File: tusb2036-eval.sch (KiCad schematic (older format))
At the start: 55 parts, among them J1 USB_B_Micro, J2 USB_A, J3 USB_A, J4 USB_A, SW1 RESET, U1 TUSB2036, U2 TPS76333, U3 TPS2044D, U4 SN75240, U5 SN75240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

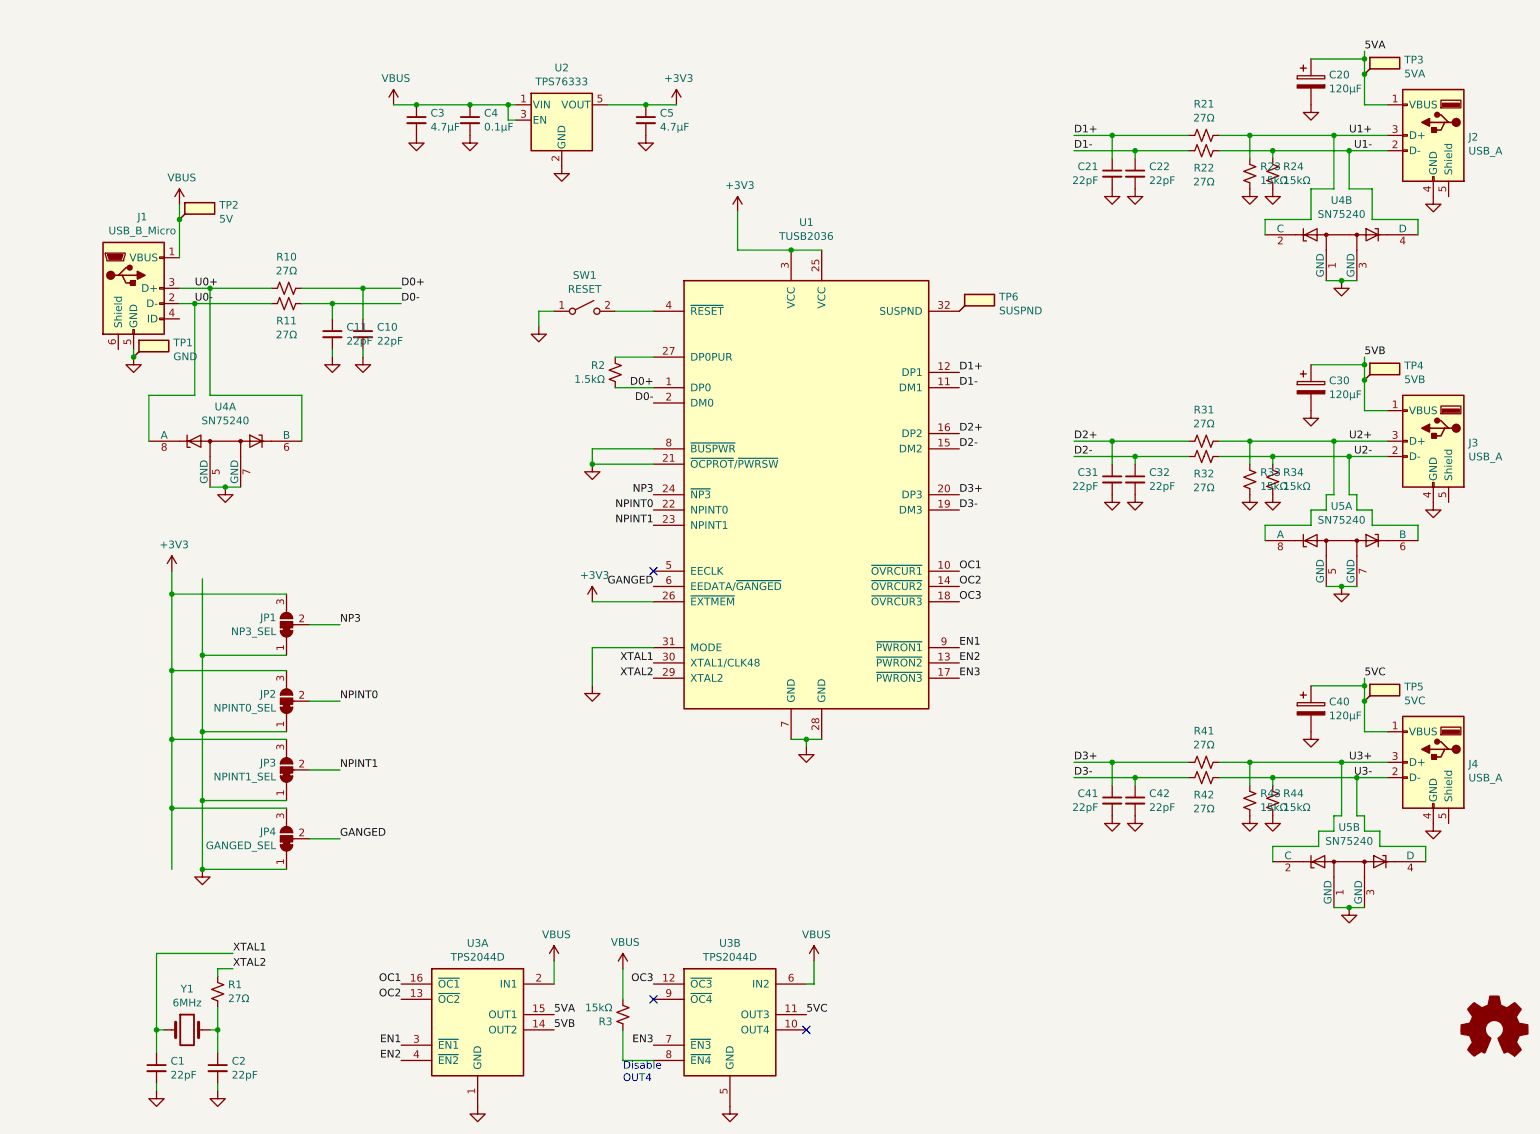
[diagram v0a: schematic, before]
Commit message: Add LEDs
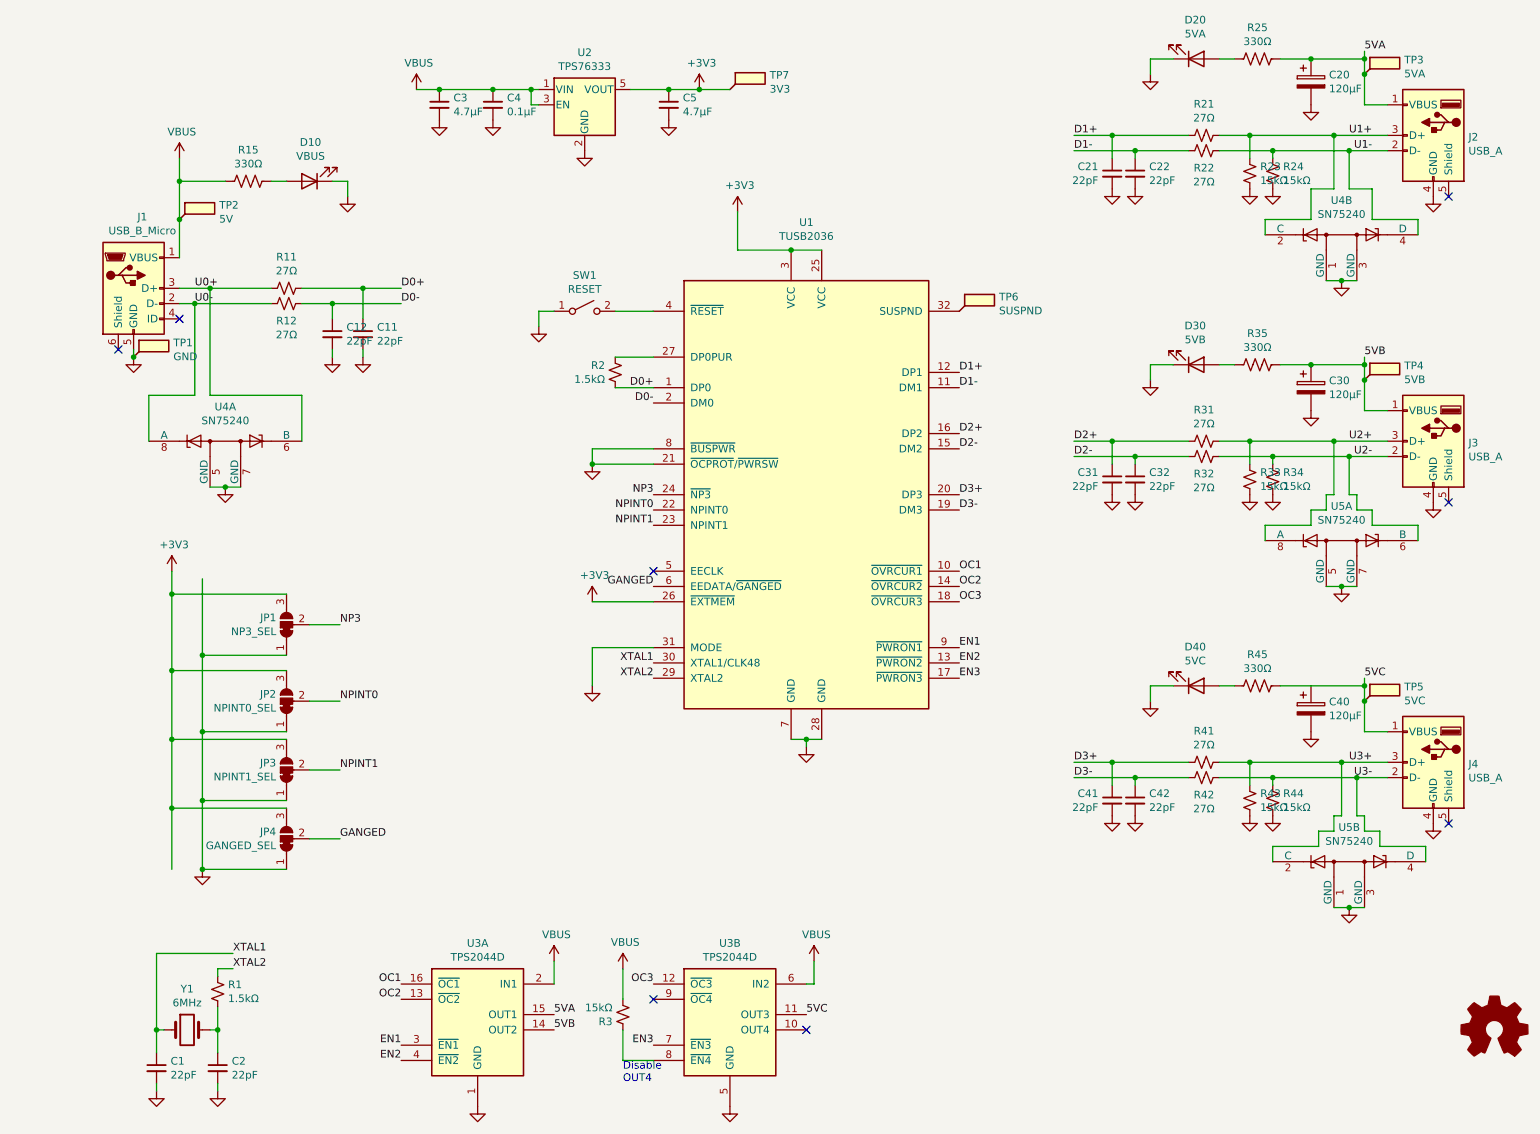
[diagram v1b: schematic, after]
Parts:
- added D10: VBUS, LED_SMD:LED_1206_3216Metric, symbol Device:LED
- added D20: 5VA, LED_SMD:LED_1206_3216Metric, symbol Device:LED
- added D30: 5VB, LED_SMD:LED_1206_3216Metric, symbol Device:LED
- added D40: 5VC, LED_SMD:LED_1206_3216Metric, symbol Device:LED
- added R15, R25, R35, R45: 330Ω, Resistor_SMD:R_1206_3216Metric, symbol Device:R_US
- added TP7: 3V3, TestPoint:TestPoint_Pad_D2.0mm, symbol Connector:TestPoint_Flag
- LOGO1, TP1, TP2, TP3, TP4, TP5: Price (none) -> 0; Vendor (none) -> -; Vendor Part # (none) -> -
- R1: value 27Ω -> 1.5kΩ; Vendor Part # 603-RC1210FR-0727RL -> 603-RC1210FR-071K5L
- renumbered C10 to C11, C11 to C12, R10 to R11, R11 to R12
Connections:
- net +3V3: now also TP7.1
- net 5VA: now also R25.1
- net 5VB: now also R35.1
- net 5VC: now also R45.1
- net GND: now also D10.1 (K), D20.1 (K), D30.1 (K), D40.1 (K)
- net VBUS: now also R15.2
- new net: D10.2 (A), R15.1
- new net: D30.2 (A), R35.2
- new net: D20.2 (A), R25.2
- new net: D40.2 (A), R45.2
- no-connect marks 3 -> 8
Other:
- moved on the sheet: C3, C4, C5, U2

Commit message: Clean up schematic
* Start using # for active-low nets
* Rearrange config block for readability
* Remove some pull-up resistors that I'm not sure about
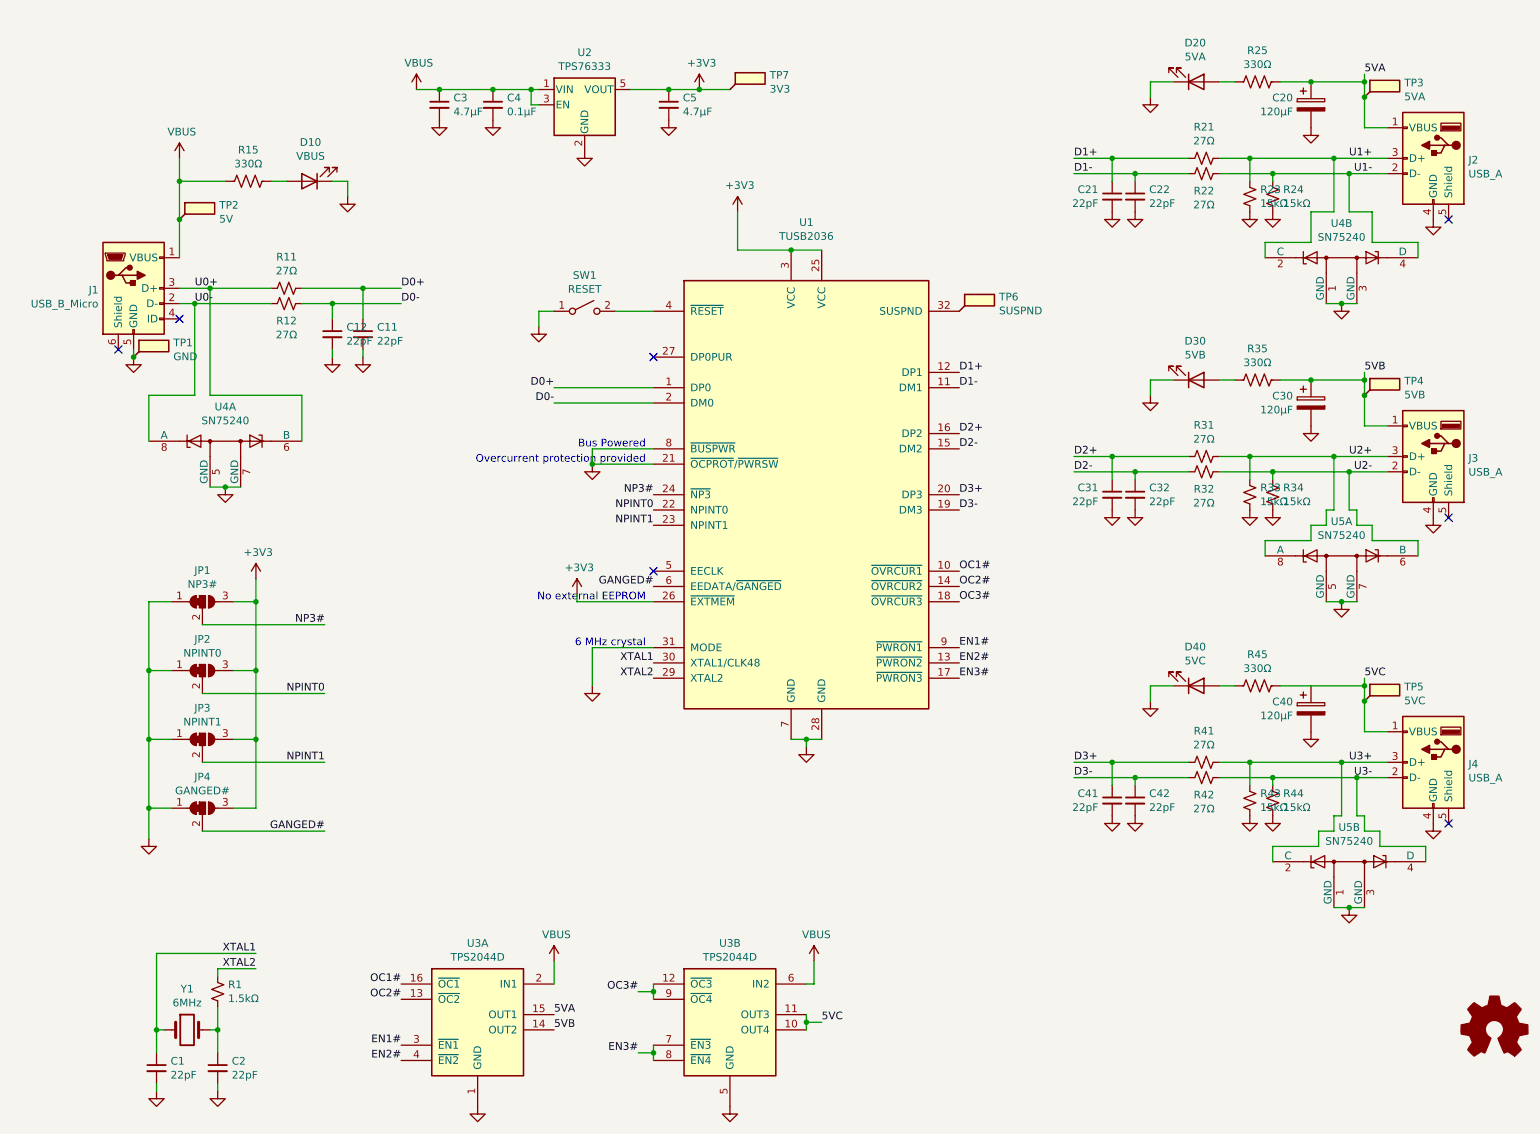
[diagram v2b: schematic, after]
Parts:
- removed R2: 1.5kΩ, Resistor_SMD:R_1206_3216Metric, symbol Device:R_Small_US
- removed R3: 15kΩ, Resistor_SMD:R_1206_3216Metric, symbol Device:R_Small_US
- JP1: value NP3_SEL -> NP3#
- JP2: value NPINT0_SEL -> NPINT0
- JP3: value NPINT1_SEL -> NPINT1
- JP4: value GANGED_SEL -> GANGED#
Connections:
- net EN3 is gone; now on net EN3#: U1.17 (~PWRON3), U3.7 (~EN3)
- net OC3 is gone; now on net OC3#: U1.18 (~OVRCUR3), U3.12 (~OC3)
- net 5VC: now also U3.10 (OUT4)
- net EN3#: now reaches U3.8 (~EN4)
- net OC3#: now reaches U3.9 (~OC4)
- net EN1 renamed EN1#
- net EN2 renamed EN2#
- net GANGED renamed GANGED#
- net NP3 renamed NP3#
- net OC1 renamed OC1#
- net OC2 renamed OC2#
- no-connect marks 8 -> 7
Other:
- note added: "6 MHz crystal"
- note added: "Bus Powered"
- note added: "No external EEPROM"
- note added: "Overcurrent protection provided"
- note removed: "Disable\nOUT4"
- moved on the sheet: C20, C21, C22, C30, C31, C32, D20, D30, J2, J3, JP1, JP2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

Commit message: Add some components from TUSB2036-EVL user guide
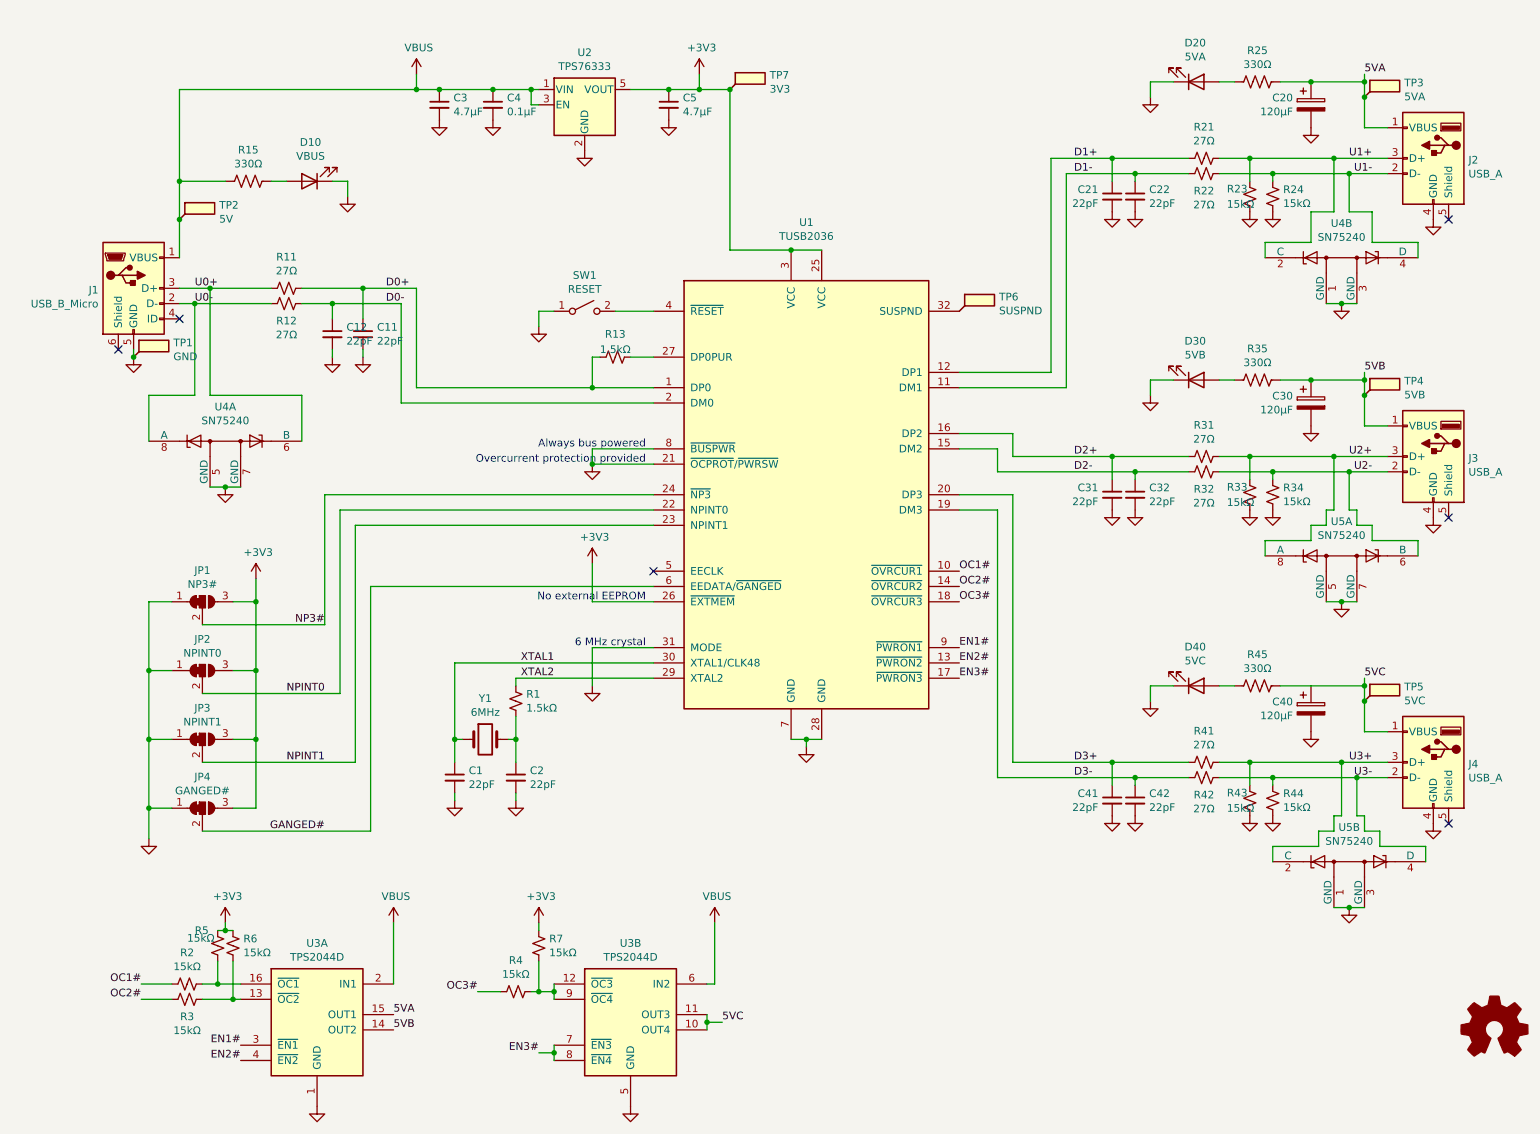
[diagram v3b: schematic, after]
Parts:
- added R13: 1.5kΩ, Resistor_SMD:R_1206_3216Metric, symbol Device:R_Small_US
- added R2, R3, R4, R5, R6, R7: 15kΩ, Resistor_SMD:R_1206_3216Metric, symbol Device:R_Small_US
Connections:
- net +3V3: now also R5.2, R6.2, R7.2
- net D0+: now also R13.2
- net OC1#: now also R2.2; no longer U3.16 (~OC1)
- net OC2#: now also R3.2; no longer U3.13 (~OC2)
- net OC3#: now also R4.2; no longer U3.12 (~OC3), U3.9 (~OC4)
- net at U1.27 (DP0PUR): now also R13.1
- new net: R3.1, R6.1, U3.13 (~OC2)
- new net: R2.1, R5.1, U3.16 (~OC1)
- new net: R4.1, R7.1, U3.12 (~OC3), U3.9 (~OC4)
- no-connect marks 7 -> 6
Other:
- note added: "Always bus powered"
- note removed: "Bus Powered"
- moved on the sheet: C1, C2, R1, U3A, U3B, Y1

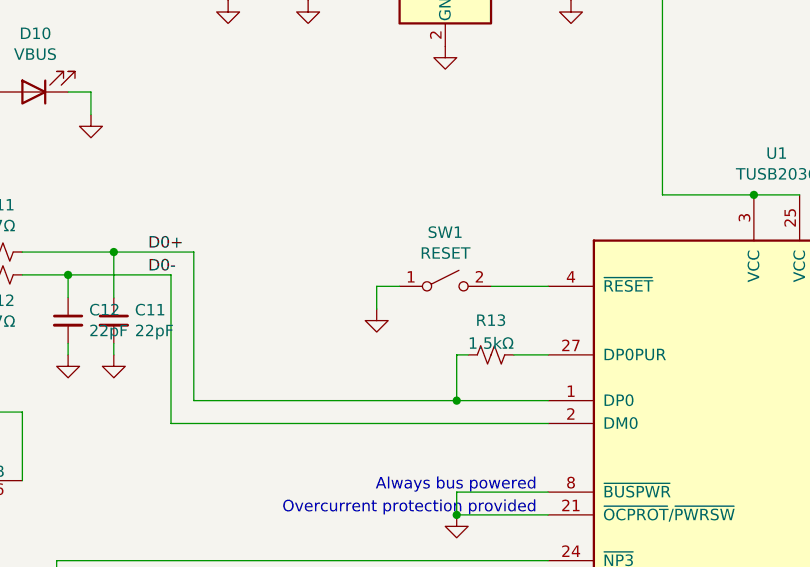
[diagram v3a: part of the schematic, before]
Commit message: Add RC filter for RESET
Suggested by eevblog user pigrew and example schematic
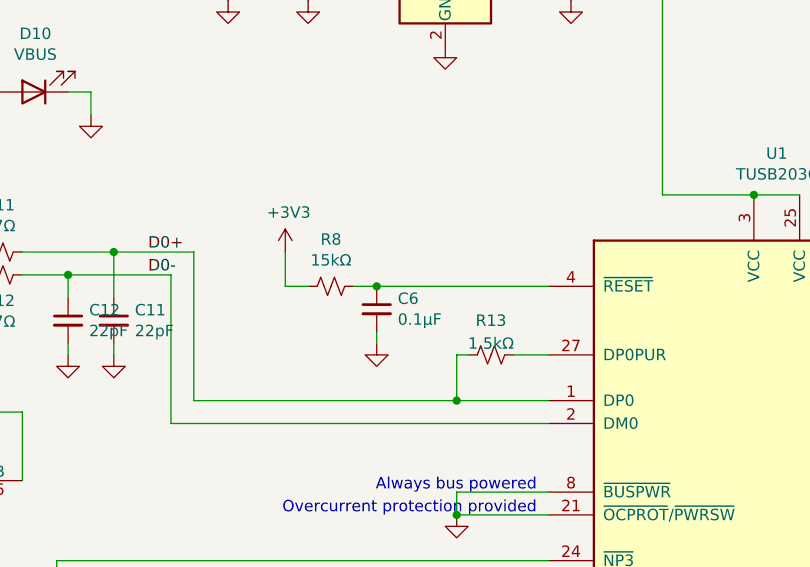
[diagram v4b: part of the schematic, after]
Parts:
- removed SW1: RESET, Omron:SW_SPST_Omron_B3FS-100xP, symbol Switch:SW_SPST
- added C6: 0.1μF, Capacitor_SMD:C_1206_3216Metric, symbol Device:C_Small
- added R8: 15kΩ, Resistor_SMD:R_1206_3216Metric, symbol Device:R_Small_US
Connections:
- net +3V3: now also R8.2
- net GND: now also C6.2
- net at U1.4 (~RESET): now also C6.1, R8.1
